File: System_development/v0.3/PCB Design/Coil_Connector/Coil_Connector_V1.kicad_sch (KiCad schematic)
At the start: 2 parts

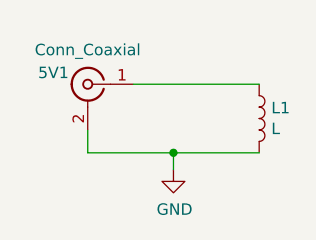
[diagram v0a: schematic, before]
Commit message: Added V2 of coil pbc and voltage regulation pcb
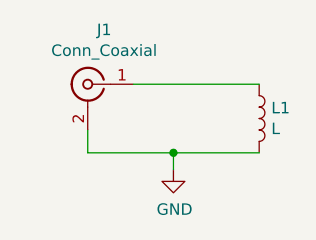
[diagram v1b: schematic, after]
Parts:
- removed 5V1: Conn_Coaxial, Connector_Coaxial:SMA_Samtec_SMA-J-P-X-ST-EM1_EdgeMount, symbol Connector:Conn_Coaxial
- added J1: Conn_Coaxial, Connector_Coaxial:SMA_Amphenol_132203-12_Horizontal, symbol Connector:Conn_Coaxial
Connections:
- net GND: now also J1.2 (Ext)
- net at L1.1: now also J1.1 (In)
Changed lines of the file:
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@@
     (stroke (width 0) (type default) (color 0 0 0 0))
+  )
+  (symbol (lib_id "Connector:Conn_Coaxial") (at 127 88.9 0) (mirror y) (unit 1)
+    (in_bom yes) (on_board yes)
+    (property "Reference" "J1" (id 0) (at 128.8288 82.8548 0))
+    (property "Value" "Conn_Coaxial" (id 1) (at 128.8288 85.1662 0))
+    (property "Footprint" "Connector_Coaxial:SMA_Amphenol_132203-12_Horizontal" (id 2) (at 127 88.9 0)
+      (effects (font (size 1.27 1.27)) hide)
+    )
+    (property "Datasheet" " ~" (id 3) (at 127 88.9 0)
+      (effects (font (size 1.27 1.27)) hide)
+    )
+    (pin "1")
+    (pin "2")
   )
   (symbol (lib_id "Device:L") (at 146.05 92.71 0) (unit 1)
@@
     (pin "1")
   )
-  (symbol (lib_id "Connector:Conn_Coaxial") (at 127 88.9 0) (mirror y) (unit 1)
-    (in_bom yes) (on_board yes)
-    (property "Reference" "5V1" (id 0) (at 123.19 87.63 0))
-    (property "Value" "Conn_Coaxial" (id 1) (at 127 85.09 0))
-    (property "Footprint" "Connector_Coaxial:SMA_Samtec_SMA-J-P-X-ST-EM1_EdgeMount" (id 2) (at 127 88.9 0)
-      (effects (font (size 1.27 1.27)) hide)
-    )
-    (property "Datasheet" " ~" (id 3) (at 127 88.9 0)
-      (effects (font (size 1.27 1.27)) hide)
-    )
-    (pin "1")
-    (pin "2")
-  )
   (sheet_instances
     (path "/" (page "1"))
@@
       (reference "#PWR01") (unit 1) (value "GND") (footprint "")
     )
-    (path "/dd9e1481-f6b4-4387-9ea1-e9f8b6be9a1a"
-      (reference "5V1") (unit 1) (value "Conn_Coaxial") (footprint "Connector_Coaxial:SMA_Samtec_SMA-J-P-X-ST-EM1_EdgeMount")
+    (path "/00000000-0000-0000-0000-000062015609"
+      (reference "J1") (unit 1) (value "Conn_Coaxial") (footprint "Connector_Coaxial:SMA_Amphenol_132203-12_Horizontal")
     )
     (path "/00000000-0000-0000-0000-00006201708a"
